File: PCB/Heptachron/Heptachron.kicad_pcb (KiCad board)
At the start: 2 copper layers, 30 x 30 mm, 11 parts, among them U1 BQ24230RGT, U2 ATtiny424-SS, U3 IS31FL3729, X1 RV-3028-C7

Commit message: Continue schematic
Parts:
- added D10: CLM, Heptachron-Lib:CREE-PLCC2-custom, F.Cu at (66.2, 79.3)
- added D11: CLM, Heptachron-Lib:CREE-PLCC2-custom, F.Cu at (66.2, 83.5)
- added D12: CLM, Heptachron-Lib:CREE-PLCC2-custom, F.Cu at (70.7, 70.8)
- added D13: CLM, Heptachron-Lib:CREE-PLCC2-custom, F.Cu at (70.7, 75.1)
- added D14: CLM, Heptachron-Lib:CREE-PLCC2-custom, F.Cu at (70.7, 79.3)
- added D15: CLM, Heptachron-Lib:CREE-PLCC2-custom, F.Cu at (55.3, 70.8)
- added D16: CLM, Heptachron-Lib:CREE-PLCC2-custom, F.Cu at (55.3, 75.1)
- added D17: CLM, Heptachron-Lib:CREE-PLCC2-custom, F.Cu at (55.3, 79.3)
- added D18: CLM, Heptachron-Lib:CREE-PLCC2-custom, F.Cu at (55.3, 83.5)
- added D19: CLM, Heptachron-Lib:CREE-PLCC2-custom, F.Cu at (59.8, 70.8)
- added D20: CLM, Heptachron-Lib:CREE-PLCC2-custom, F.Cu at (59.8, 75.1)
- added D21: CLM, Heptachron-Lib:CREE-PLCC2-custom, F.Cu at (59.8, 79.3)
- added D22: CLM, Heptachron-Lib:CREE-PLCC2-custom, F.Cu at (66.2, 52.0)
- added D23: CLM, Heptachron-Lib:CREE-PLCC2-custom, F.Cu at (66.2, 56.2)
- added D24: CLM, Heptachron-Lib:CREE-PLCC2-custom, F.Cu at (66.2, 60.4)
- added D25: CLM, Heptachron-Lib:CREE-PLCC2-custom, F.Cu at (66.2, 64.6)
- added D26: CLM, Heptachron-Lib:CREE-PLCC2-custom, F.Cu at (70.7, 52.0)
- added D27: CLM, Heptachron-Lib:CREE-PLCC2-custom, F.Cu at (70.7, 56.2)
- added D28: CLM, Heptachron-Lib:CREE-PLCC2-custom, F.Cu at (70.7, 60.4)
- added D29: CLM, Heptachron-Lib:CREE-PLCC2-custom, F.Cu at (55.3, 52.0)
- added D30: CLM, Heptachron-Lib:CREE-PLCC2-custom, F.Cu at (55.3, 56.2)
- added D31: CLM, Heptachron-Lib:CREE-PLCC2-custom, F.Cu at (55.3, 60.4)
- added D32: CLM, Heptachron-Lib:CREE-PLCC2-custom, F.Cu at (55.3, 64.6)
- added D33: CLM, Heptachron-Lib:CREE-PLCC2-custom, F.Cu at (59.8, 52.0)
- added D34: CLM, Heptachron-Lib:CREE-PLCC2-custom, F.Cu at (59.8, 56.2)
- added D35: CLM, Heptachron-Lib:CREE-PLCC2-custom, F.Cu at (59.8, 60.4)
- added D36: CLM, LED_SMD:LED_0603_1608Metric, F.Cu at (76.8, 69.5)
- added D37: CLM, LED_SMD:LED_0603_1608Metric, F.Cu at (76.8, 72.1)
- added D8: CLM, Heptachron-Lib:CREE-PLCC2-custom, F.Cu at (66.2, 70.8)
- added D9: CLM, Heptachron-Lib:CREE-PLCC2-custom, F.Cu at (66.2, 75.1)
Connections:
- U3 pad 1: unconnected-(U3-CS4-Pad1) -> /CS4
- U3 pad 15: unconnected-(U3-SW8-Pad15) -> /SW8
- U3 pad 16: unconnected-(U3-SW7-Pad16) -> /SW7
- U3 pad 17: unconnected-(U3-SW6-Pad17) -> /SW6
- U3 pad 18: unconnected-(U3-SW5-Pad18) -> /SW5
- U3 pad 19: unconnected-(U3-SW4-Pad19) -> /SW4
- U3 pad 2: unconnected-(U3-CS5-Pad2) -> /CS5
- U3 pad 20: unconnected-(U3-SW3-Pad20) -> /SW3
- U3 pad 21: unconnected-(U3-SW2-Pad21) -> /SW2
- U3 pad 22: unconnected-(U3-SW1-Pad22) -> /SW1
- U3 pad 3: unconnected-(U3-CS6-Pad3) -> /CS6
- U3 pad 30: unconnected-(U3-CS1-Pad30) -> /CS1
- U3 pad 31: unconnected-(U3-CS2-Pad31) -> /CS2
- U3 pad 32: unconnected-(U3-CS3-Pad32) -> /CS3
- U3 pad 4: unconnected-(U3-CS7-Pad4) -> /CS7

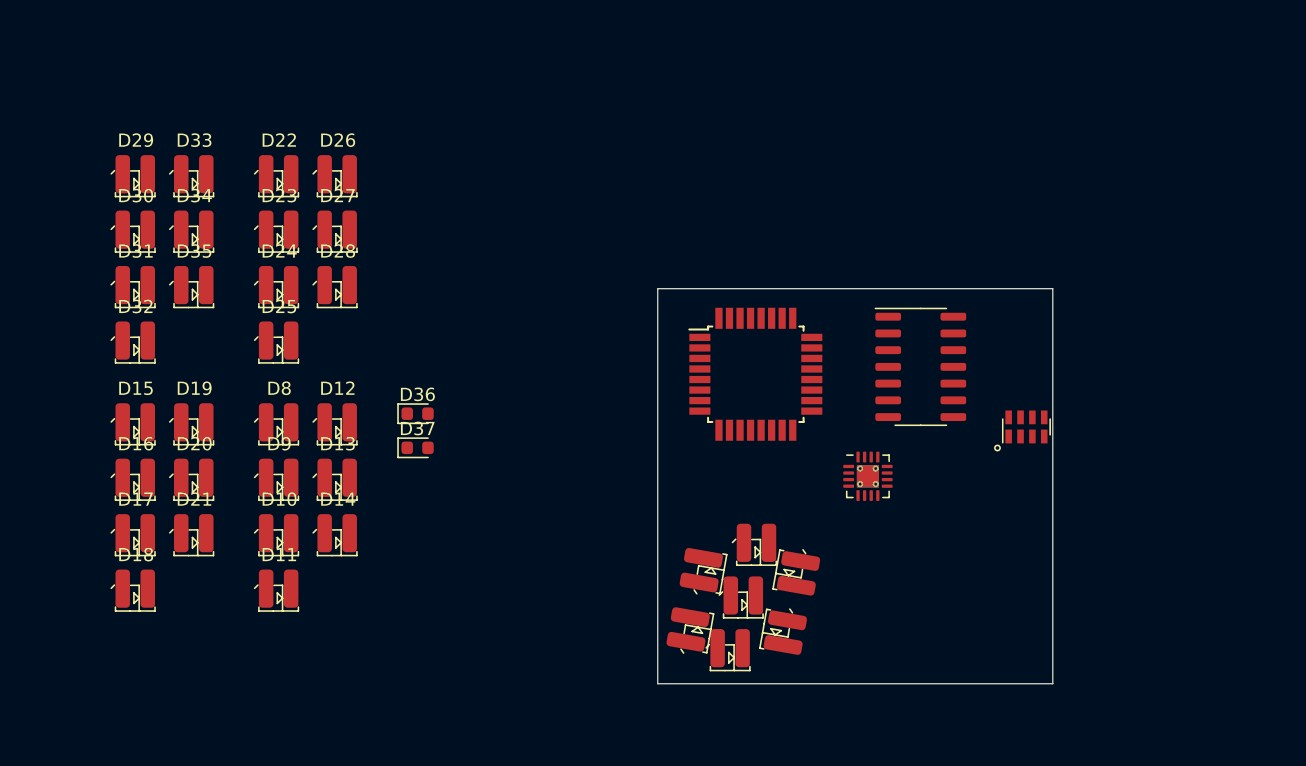
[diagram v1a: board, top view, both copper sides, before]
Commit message: Continue schematic, symbols & footprints for digits
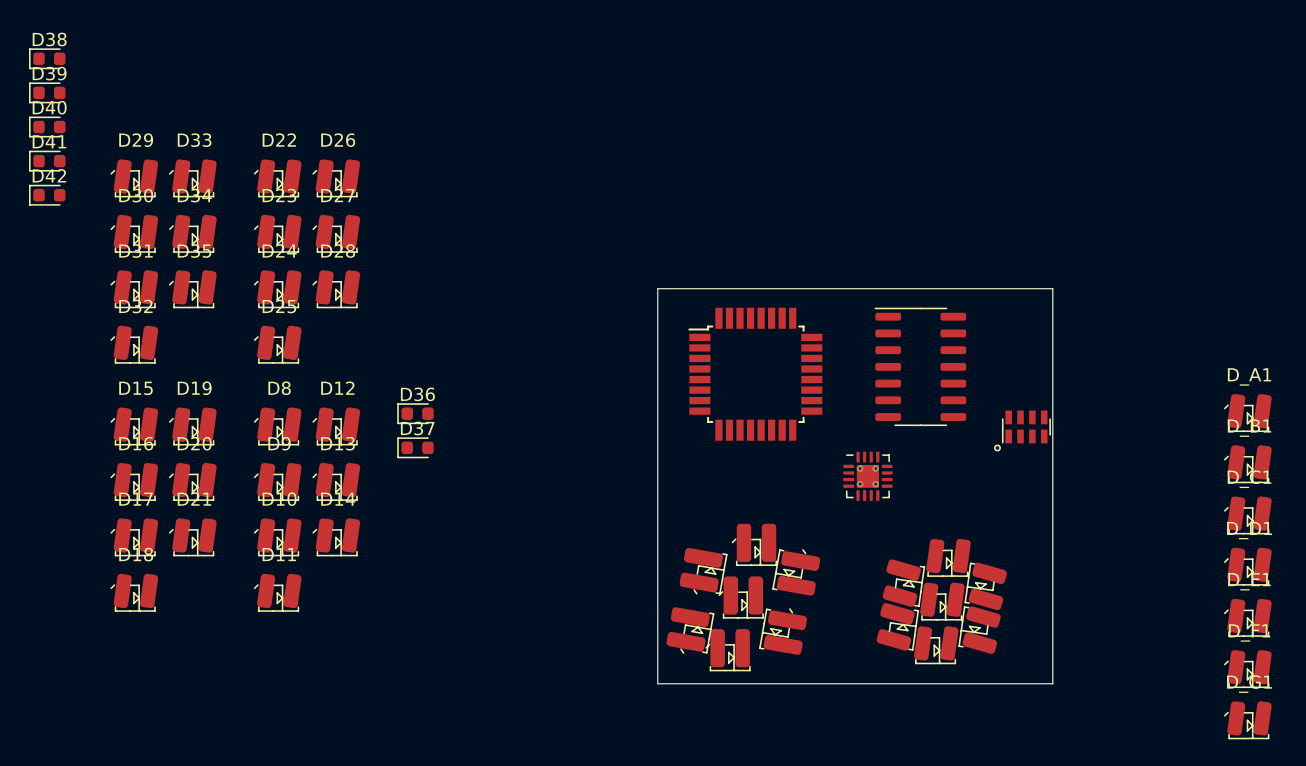
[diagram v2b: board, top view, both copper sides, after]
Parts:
- added D38: ~, LED_SMD:LED_0603_1608Metric, F.Cu at (48.8, 42.5)
- added D39: ~, LED_SMD:LED_0603_1608Metric, F.Cu at (48.8, 45.1)
- added D40: ~, LED_SMD:LED_0603_1608Metric, F.Cu at (48.8, 47.7)
- added D41: ~, LED_SMD:LED_0603_1608Metric, F.Cu at (48.8, 50.3)
- added D42: ~, LED_SMD:LED_0603_1608Metric, F.Cu at (48.8, 52.9)
- added D_A1: CLM, Heptachron-Lib:CREE-PLCC2-angled, F.Cu at (139.9, 69.8)
- added D_B1: CLM, Heptachron-Lib:CREE-PLCC2-angled, F.Cu at (139.9, 73.7)
- added D_C1: CLM, Heptachron-Lib:CREE-PLCC2-angled, F.Cu at (139.9, 77.6)
- added D_D1: CLM, Heptachron-Lib:CREE-PLCC2-angled, F.Cu at (139.9, 81.5)
- added D_E1: CLM, Heptachron-Lib:CREE-PLCC2-angled, F.Cu at (139.9, 85.4)
- added D_F1: CLM, Heptachron-Lib:CREE-PLCC2-angled, F.Cu at (139.9, 89.3)
- added D_G1: CLM, Heptachron-Lib:CREE-PLCC2-angled, F.Cu at (139.9, 93.2)
- added U4: ~, Heptachron-Lib:7-segment-digit-Cree, F.Cu at (116.6, 84.2)
- D10, D11, D12, D13, D14, D15, D16, D17, D18, D19, D20, D21, D22, D23, D24, D25, D26, D27, D28, D29, D30, D31, D32, D33, D34, D35, D8, D9: footprint Heptachron-Lib:CREE-PLCC2-custom -> Heptachron-Lib:CREE-PLCC2-angled
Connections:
- D36 pad 1: unconnected-(D36-K-Pad1) -> /CS4
- D36 pad 2: unconnected-(D36-A-Pad2) -> /SW6
- D37 pad 1: unconnected-(D37-K-Pad1) -> /CS4
- D37 pad 2: unconnected-(D37-A-Pad2) -> /SW7

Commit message: PCB work and 3D modeling
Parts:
- added U2: ~, Heptachron-Lib:7-segment-digit-Cree, F.Cu at (142.0, 101.0)
- added U3: ~, Heptachron-Lib:7-segment-digit-Cree, F.Cu at (154.0, 101.0)
- added U4: ~, Heptachron-Lib:7-segment-digit-Cree, F.Cu at (163.5, 101.0)
- moved D42 117.0 mm to (152.0, 108.0), turned to 90 degrees
- moved D41 116.5 mm to (150.0, 108.0), turned to 90 degrees
- moved D40 116.1 mm to (148.0, 108.0), turned to 90 degrees
- moved D39 115.8 mm to (146.0, 108.0), turned to 90 degrees
- moved D38 115.5 mm to (144.0, 108.0), turned to 90 degrees
- moved D_A1 111.4 mm to (28.9, 79.3)
- moved D_B1 111.4 mm to (28.9, 83.2)
- moved D_C1 111.4 mm to (28.9, 87.1)
- moved D_D1 111.4 mm to (28.9, 91.0)
- moved D_E1 111.4 mm to (28.9, 94.9)
- moved D_F1 111.4 mm to (28.9, 98.8)
- moved D_G1 111.4 mm to (28.9, 102.7)
- moved D37 77.5 mm to (148.0, 102.6), turned to -90 degrees
- moved D36 77.3 mm to (148.0, 99.4), turned to 90 degrees
- moved D1 61.8 mm to (72.5, 26.0)
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- renumbered U4 to U1, U1 to U6, U3 to U7, U2 to U8
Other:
- board size 30 x 30 mm -> 44 x 34 mm

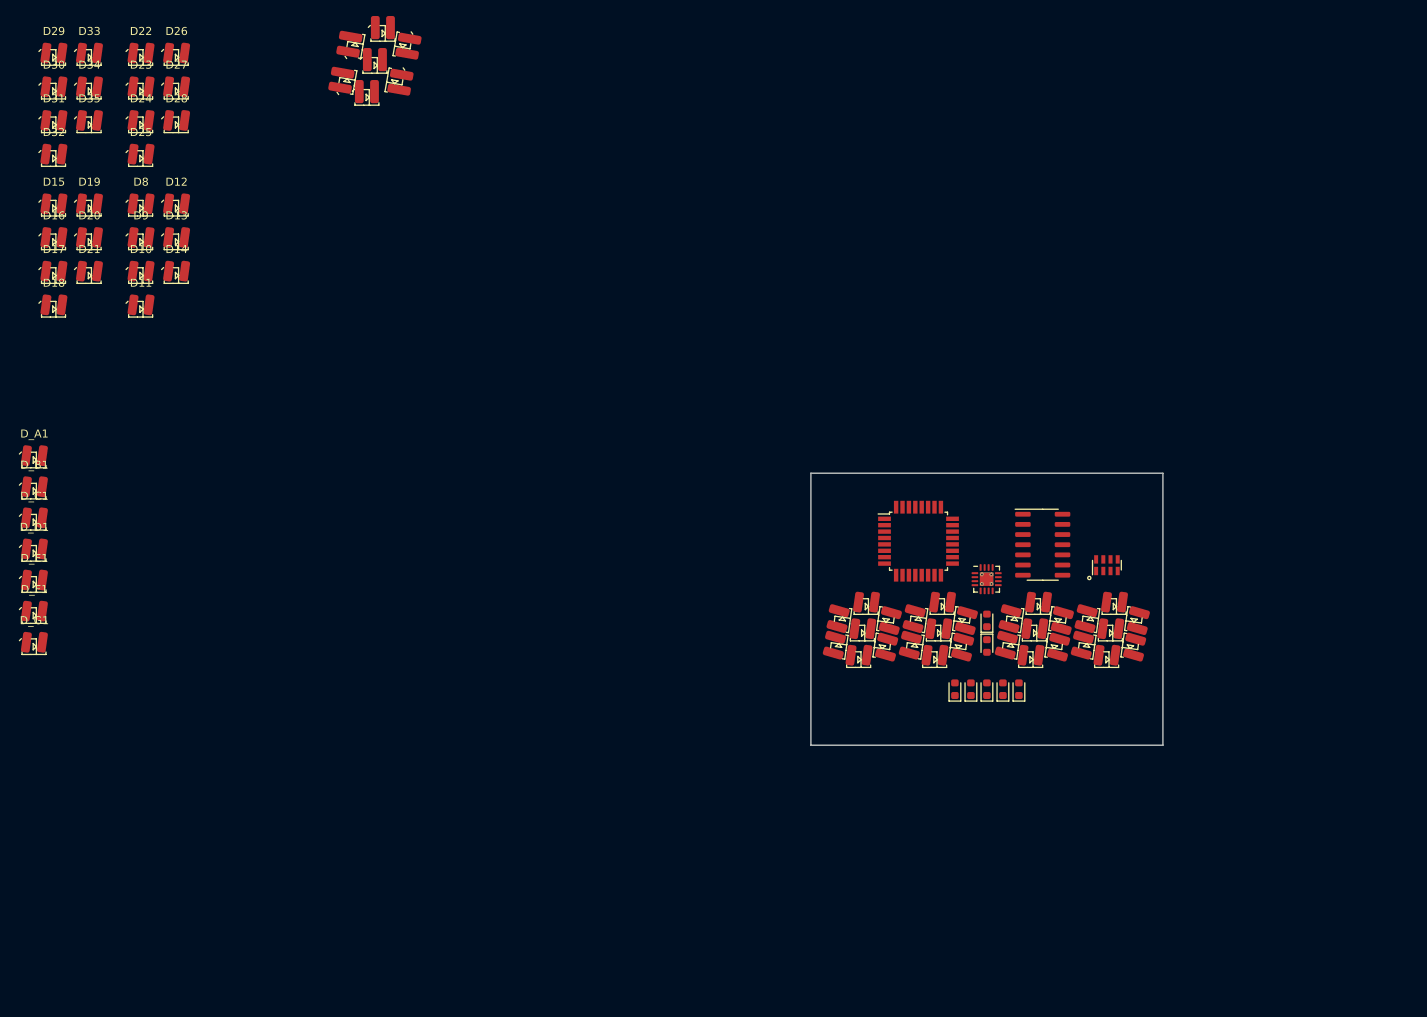
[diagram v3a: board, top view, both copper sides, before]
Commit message: Finish test PCB [Ordered]
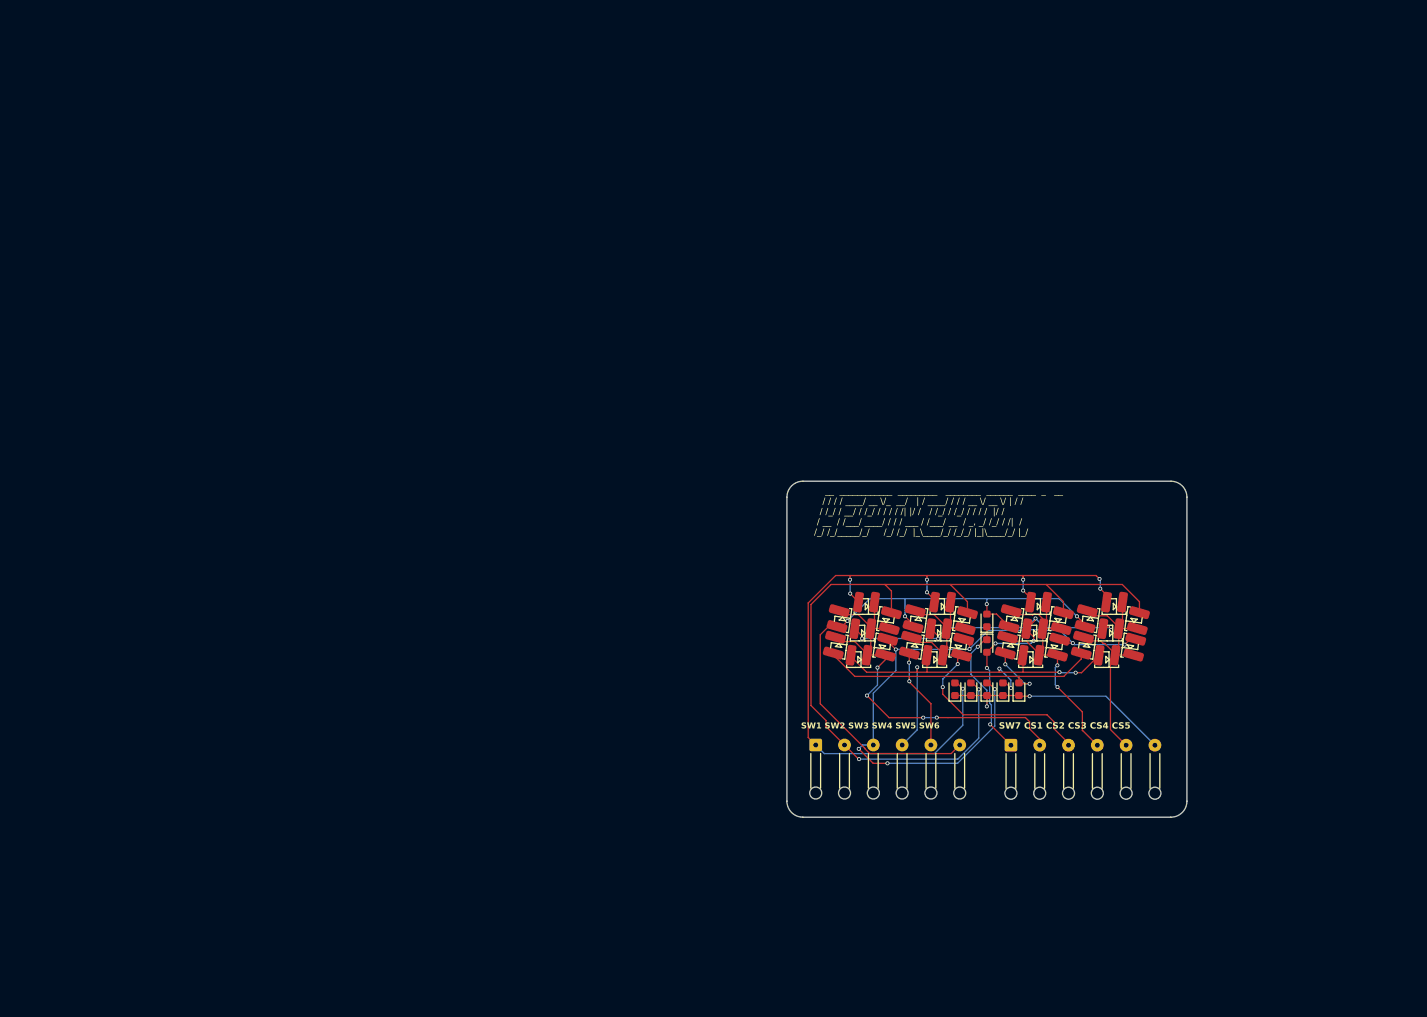
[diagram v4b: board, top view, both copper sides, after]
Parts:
- removed D1, D2, D3, D4, D5, D6, D7: CLM, Heptachron-Lib:CREE-PLCC2-custom
- removed D10, D11, D12, D13, D14, D15, D16, D17, D18, D19, D20, D21, D22, D23, D24, D25, D26, D27, D28, D29, D30, D31, D32, D33, D34, D35, D8, D9, D_A1, D_B1, D_C1, D_D1, D_E1, D_F1, D_G1: CLM, Heptachron-Lib:CREE-PLCC2-angled
- removed U6: BQ24230RGT, Package_DFN_QFN:VQFN-16-1EP_3x3mm_P0.5mm_EP1.68x1.68mm_ThermalVias
- removed U7: IS31FL3729, Package_QFP:TQFP-32_7x7mm_P0.8mm
- removed U8: ATtiny424-SS, Package_SO:SOIC-14_3.9x8.7mm_P1.27mm
- removed X1: RV-3028-C7, Heptachron-Lib:RV-3028-C7
- added J1: Conn_01x06_Pin, Connector_Wire:SolderWire-0.1sqmm_1x06_P3.6mm_D0.4mm_OD1mm_Relief, F.Cu at (126.6, 115.0)
- added J2: Conn_01x06_Pin, Connector_Wire:SolderWire-0.1sqmm_1x06_P3.6mm_D0.4mm_OD1mm_Relief, F.Cu at (151.0, 115.0)
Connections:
- D36 pad 1: /CS4 -> /CS5
- D37 pad 1: /CS4 -> /CS5
- D38 pad 1: /CS4 -> /CS5
- D39 pad 1: /CS4 -> /CS5
- D40 pad 1: /CS4 -> /CS5
- D41 pad 1: /CS4 -> /CS5
- D42 pad 1: /CS4 -> /CS5
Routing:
- net /SW2: track 0.00 -> 102.4 mm, vias 0 -> 2
- net /SW1: track 0.00 -> 96.8 mm, vias 0 -> 9
- net /SW3: track 0.00 -> 77.9 mm, vias 0 -> 7
- net /SW6: track 0.00 -> 74.9 mm, vias 0 -> 4
- net /SW7: track 0.00 -> 60.1 mm, vias 0 -> 8
- net /SW5: track 0.00 -> 54.9 mm, vias 0 -> 4
- net /SW4: track 0.00 -> 53.1 mm, vias 0 -> 5
- net /CS1: track 0.00 -> 52.8 mm, vias 0 -> 4
- net /CS2: track 0.00 -> 46.5 mm, vias 0 -> 2
- net /CS5: track 0.00 -> 40.7 mm, vias 0 -> 3
- net /CS3: track 0.00 -> 36.8 mm, vias 0 -> 2
- net /CS4: track 0.00 -> 33.9 mm
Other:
- board size 44 x 34 mm -> 50 x 42 mm
- board text added: "SW1 SW2 SW3 SW4 SW5 SW6"
- board text added: "SW7 CS1 CS2 CS3 CS4 CS5"
- board text added: "__ ____________ _________ ________ ______ ____ _ __ / / / / ____/ __ \/_ __/ | / ____/ / / / __ \/ __ \/ | / / / /_/ / __/ / /_/ / / / / /| |/ / / /_/ / /_/ / / / / |/ / / __ / /___/ ____/ / / / ___ / /___/ __ / _, _/ /_/ / /| / /_/ /_/_____/_/ /_/ /_/ |_\____/_/ /_/_/ |_|\____/_/ |_/"
